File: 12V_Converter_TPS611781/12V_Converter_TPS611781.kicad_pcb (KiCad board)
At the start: 2 copper layers, 40.3 x 27.2 mm, 25 parts, among them M1 IQE050N08NM5CGSC, U1 LM51561HPWPR

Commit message: updated cvcc orientation
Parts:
- turned Cvcc1 to 90 degrees
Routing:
- net Net-(Cvcc1-Pad1): track 5.82 -> 4.43 mm
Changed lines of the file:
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@@
   )
   (footprint "Capacitor_SMD:C_0603_1608Metric" (layer "F.Cu")
-    (at 80.518 106.667 -90)
+    (at 80.518 106.667 90)
     (descr "Capacitor SMD 0603 (1608 Metric), square (rectangular) end terminal, IPC_7351 nominal, (Body size source: IPC-SM-782 page 76, https://www.pcb-3d.com/wordpress/wp-content/uploads/ipc-sm-782a_amendment_1_and_2.pdf), generated with kicad-footprint-generator")
     (tags "capacitor")
@@
     (fp_line (start 0.8 -0.4) (end 0.8 0.4) (layer "F.Fab") (width 0.1))
     (fp_line (start -0.8 -0.4) (end 0.8 -0.4) (layer "F.Fab") (width 0.1))
-    (pad "1" smd roundrect (at -0.775 0 270) (size 0.9 0.95) (layers "F.Cu" "F.Paste" "F.Mask") (roundrect_rratio 0.25)
+    (pad "1" smd roundrect (at -0.775 0 90) (size 0.9 0.95) (layers "F.Cu" "F.Paste" "F.Mask") (roundrect_rratio 0.25)
       (net 8 "Net-(Cvcc1-Pad1)") (pintype "passive"))
-    (pad "2" smd roundrect (at 0.775 0 270) (size 0.9 0.95) (layers "F.Cu" "F.Paste" "F.Mask") (roundrect_rratio 0.25)
+    (pad "2" smd roundrect (at 0.775 0 90) (size 0.9 0.95) (layers "F.Cu" "F.Paste" "F.Mask") (roundrect_rratio 0.25)
       (net 2 "GND") (pintype "passive"))
     (model "${KICAD6_3DMODEL_DIR}/Capacitor_SMD.3dshapes/C_0603_1608Metric.wrl"
@@
   (segment (start 82.677 118.11) (end 79.248 118.11) (width 1) (layer "F.Cu") (net 6))
   (segment (start 89.601334 109.855) (end 92.456 109.855) (width 0.4) (layer "F.Cu") (net 7))
-  (segment (start 82.661999 109.204999) (end 82.296 108.839) (width 0.25) (layer "F.Cu") (net 8))
-  (segment (start 82.296 108.437784) (end 81.407 107.548784) (width 0.25) (layer "F.Cu") (net 8))
-  (segment (start 81.254 105.892) (end 80.518 105.892) (width 0.25) (layer "F.Cu") (net 8))
-  (segment (start 82.296 108.839) (end 82.296 108.437784) (width 0.25) (layer "F.Cu") (net 8))
-  (segment (start 81.407 106.045) (end 81.254 105.892) (width 0.25) (layer "F.Cu") (net 8))
   (segment (start 83.850566 109.204999) (end 82.661999 109.204999) (width 0.25) (layer "F.Cu") (net 8))
-  (segment (start 81.407 107.548784) (end 81.407 106.045) (width 0.25) (layer "F.Cu") (net 8))
+  (segment (start 81.915 108.458) (end 80.899 108.458) (width 0.25) (layer "F.Cu") (net 8))
+  (segment (start 80.518 108.077) (end 80.518 107.442) (width 0.25) (layer "F.Cu") (net 8))
+  (segment (start 82.661999 109.204999) (end 81.915 108.458) (width 0.25) (layer "F.Cu") (net 8))
+  (segment (start 80.899 108.458) (end 80.518 108.077) (width 0.25) (layer "F.Cu") (net 8))
   (segment (start 73.364999 114.323501) (end 72.715001 114.323501) (width 1.25) (layer "F.Cu") (net 9))
   (segment (start 72.715001 114.323501) (end 72.064999 114.323501) (width 1.25) (layer "F.Cu") (net 9))

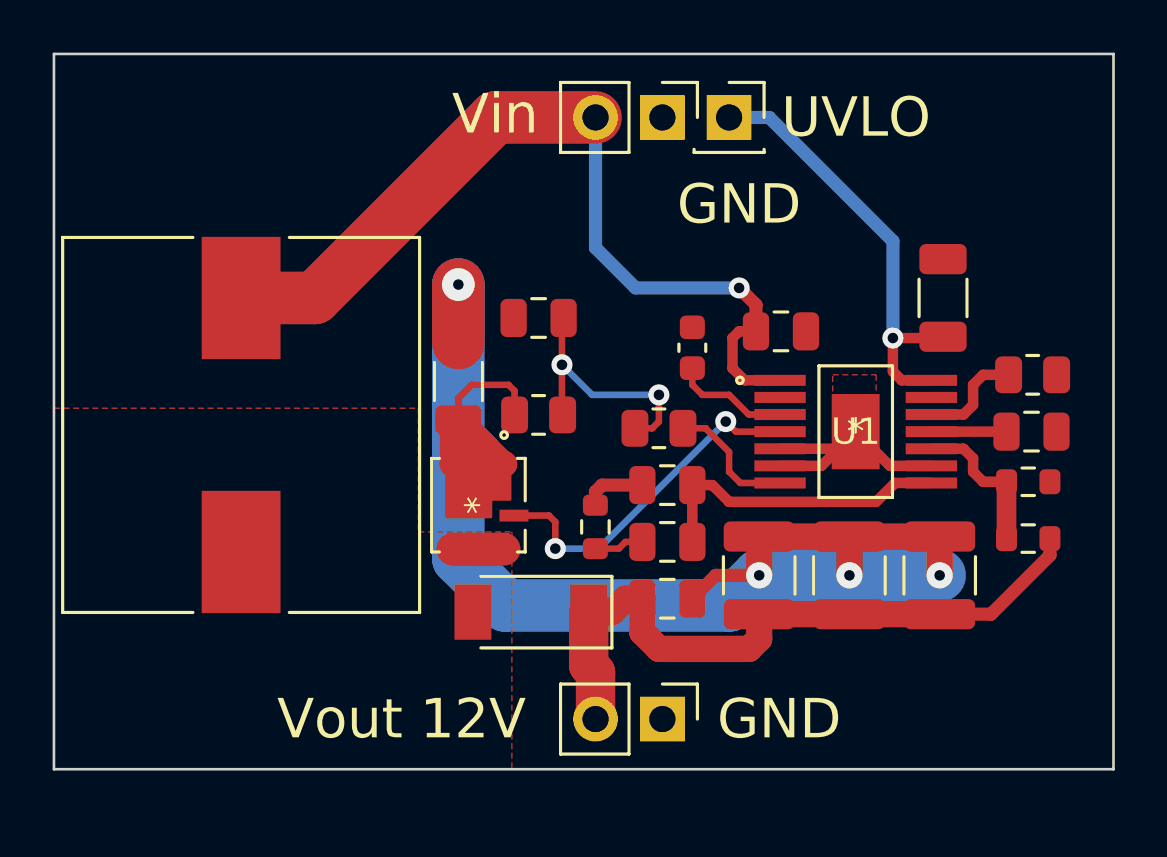
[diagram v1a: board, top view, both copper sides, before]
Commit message: closed closer loop
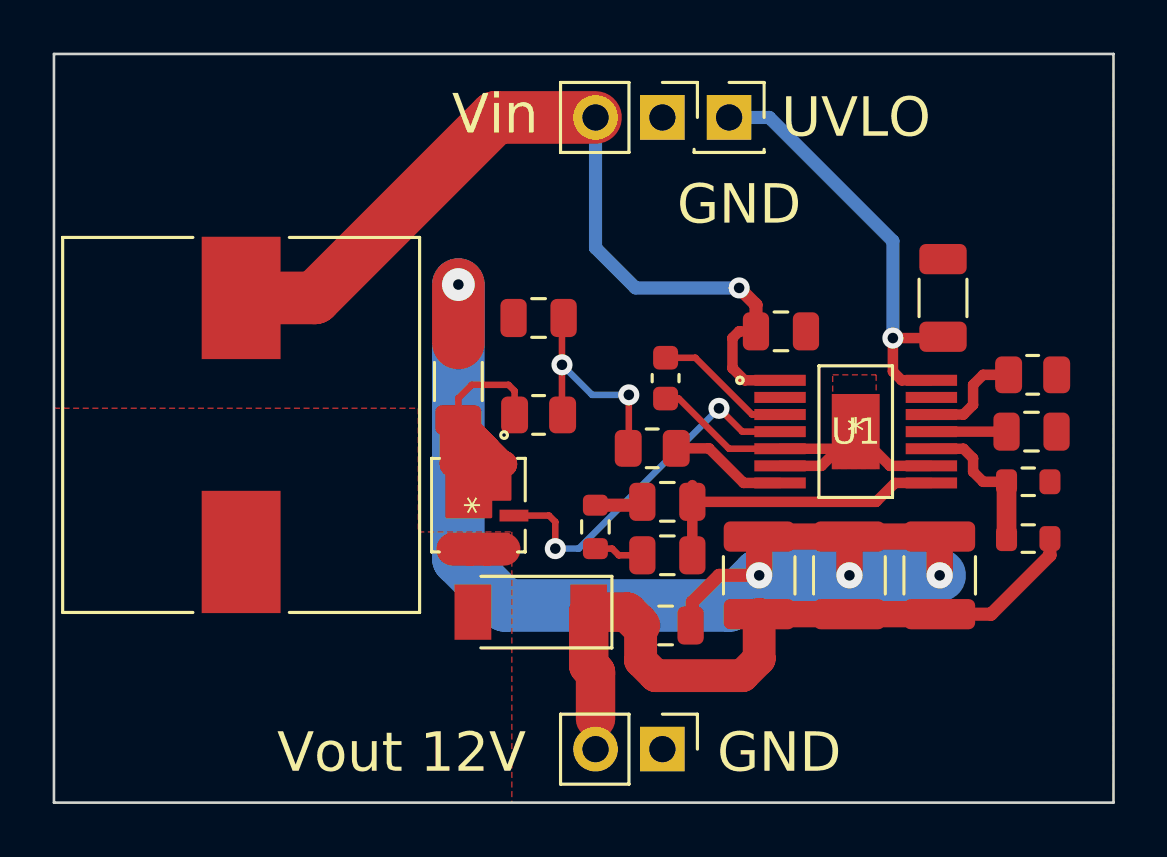
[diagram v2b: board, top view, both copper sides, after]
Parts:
- moved Cvcc1 1.54 mm to (79.5, 107.8), turned to -90 degrees
- moved REF 1.14 mm to (79.4, 121.9)
- moved Coutx1 1.02 mm to (79.5, 117.2)
- moved Rsl1 0.80 mm to (79.0, 110.5)
- moved Ccomp2 0.64 mm to (79.6, 112.5)
- moved Ccomp1 0.51 mm to (79.6, 114.6)
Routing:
- net GND: track 58.7 -> 64.2 mm
- net Net-(Ccs1-Pad1): track 9.78 -> 8.65 mm
- net Vout: track 26.1 -> 27.0 mm
- net Net-(Cvcc1-Pad1): track 4.43 -> 5.24 mm
- net Net-(Rsl1-Pad1): track 5.00 -> 4.49 mm
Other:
- board size 40.3 x 27.2 mm -> 40.3 x 28.4 mm

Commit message: shifted some things over to the right and got rid of the ground river in the middle
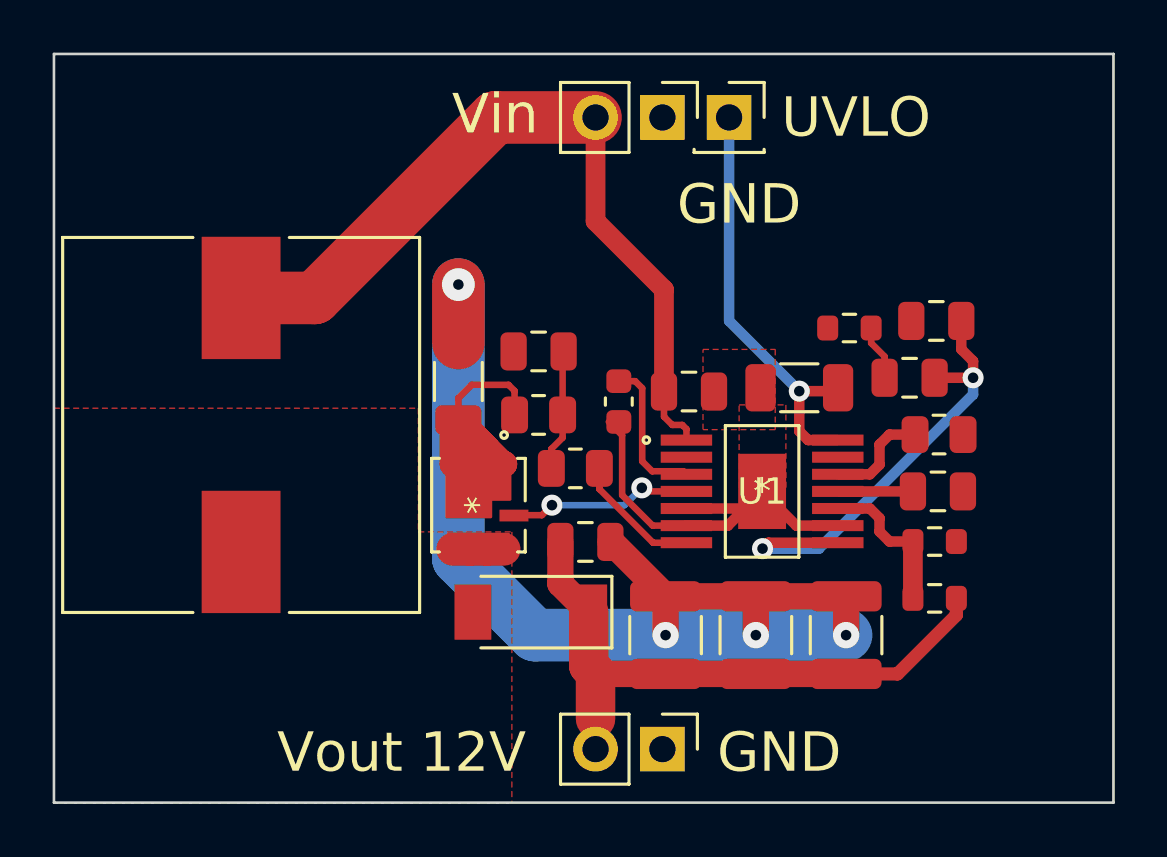
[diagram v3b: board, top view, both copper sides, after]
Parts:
- moved Ccomp2 12.3 mm to (89.8, 105.6)
- moved Rcomp1 12.3 mm to (86.5, 105.9), turned to 0 degrees
- moved Ccomp1 11.4 mm to (88.8, 107.8)
- moved Cin1 6.44 mm to (84.6, 108.2), turned to 0 degrees
- moved Coutx1 4.40 mm to (76.5, 114.0)
- moved Cout1 4.22 mm to (79.5, 117.6)
- moved Cout2 4.22 mm to (86.4, 117.6)
- moved Cout3 4.22 mm to (82.9, 117.6)
- moved Rfbt1 4.22 mm to (89.7, 116.2)
- moved Rt1 4.22 mm to (89.9, 110.0)
- moved Css1 4.22 mm to (89.8, 112.1)
- moved Rfbb1 4.22 mm to (89.7, 114.0)
- moved U1 4.22 mm to (83.2, 112.1)
- moved Cbias1 4.18 mm to (80.4, 108.3)
- moved Rsl1 3.02 mm to (76.1, 111.3)
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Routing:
- net Net-(M1-Pad9): track 13.8 -> 7.05 mm
- net Net-(Ccomp1-Pad2): track 12.0 -> 17.8 mm, vias 0 -> 2
- net GND: track 64.2 -> 58.7 mm
- net Vout: track 27.0 -> 22.6 mm
- net Net-(Ccs1-Pad1): track 8.65 -> 4.64 mm, vias 2 -> 0
- net Vin: track 33.4 -> 30.2 mm, vias 1 -> 0

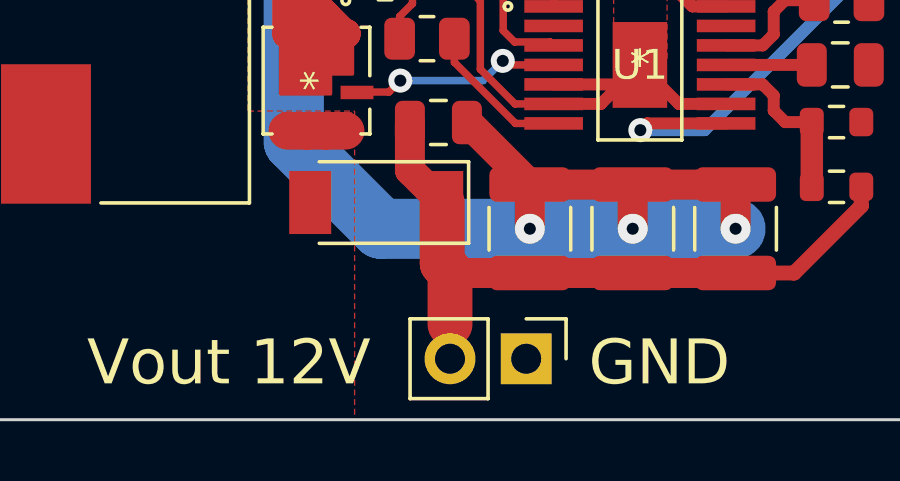
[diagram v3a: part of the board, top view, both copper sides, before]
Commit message: shifted trace to actually align with vout lolololololo
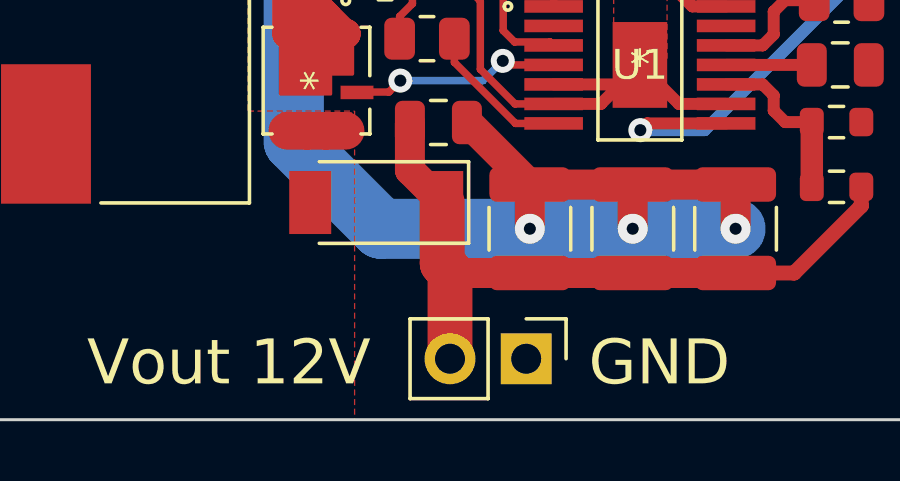
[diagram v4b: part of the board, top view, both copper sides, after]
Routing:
- net Vout: track 22.6 -> 23.7 mm
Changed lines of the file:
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@@
   (segment (start 82.930742 119.061999) (end 79.501742 119.061999) (width 1) (layer "F.Cu") (net 6))
   (segment (start 75.504 115.636) (end 75.504 114.046) (width 1) (layer "F.Cu") (net 6))
+  (segment (start 76.84 119.004) (end 76.84 121.92) (width 1.5) (layer "F.Cu") (net 6))
   (segment (start 76.581 118.745) (end 76.84 119.004) (width 1.5) (layer "F.Cu") (net 6))
   (segment (start 76.581 116.713) (end 75.504 115.636) (width 1) (layer "F.Cu") (net 6))
   (segment (start 88.313742 119.061999) (end 86.359742 119.061999) (width 0.5) (layer "F.Cu") (net 6))
-  (segment (start 76.84 119.004) (end 76.84 120.777) (width 1.5) (layer "F.Cu") (net 6))
   (segment (start 86.045076 112.125999) (end 88.899742 112.125999) (width 0.4) (layer "F.Cu") (net 7))
   (segment (start 78.613 108.204) (end 78.346 107.937) (width 0.25) (layer "F.Cu") (net 8))
